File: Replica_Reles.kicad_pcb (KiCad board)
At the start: 2 copper layers, 60 x 145 mm, 70 parts, among them J1 Bornera, J2 Bornera, J3 Tira de Pines Macho, J4 Bornera, J5 Bornera, J6 Bornera, J7 Bornera, J8 Bornera, J9 Bornera, K1 SONGLE_SRD_Form_C, K2 SONGLE_SRD_Form_C, K3 SONGLE_SRD_Form_C, K4 SONGLE_SRD_Form_C, K5 SONGLE_SRD_Form_C, K6 SONGLE_SRD_Form_C, K7 SONGLE_SRD_Form_C, K8 SONGLE_SRD_Form_C, Q1 S8050, Q2 S8050, Q3 S8050, Q4 S8050, Q5 S8050, Q6 S8050, Q7 S8050, Q8 S8050, U1 PC817, U2 PC817, U3 PC817, U4 PC817, U5 PC817, U6 PC817, U7 PC817, U8 PC817

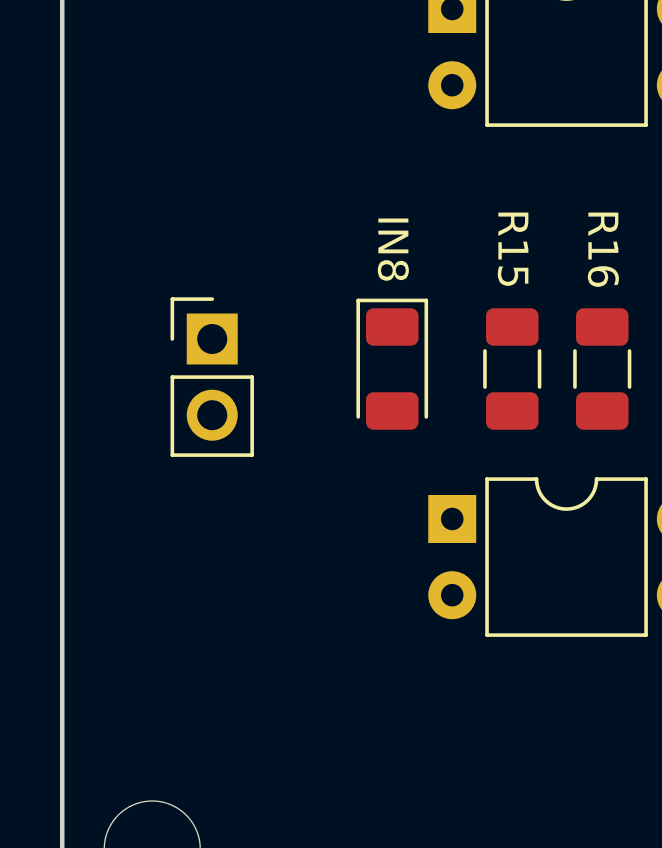
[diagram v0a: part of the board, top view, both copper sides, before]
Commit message: Arreglo de modelos 3D
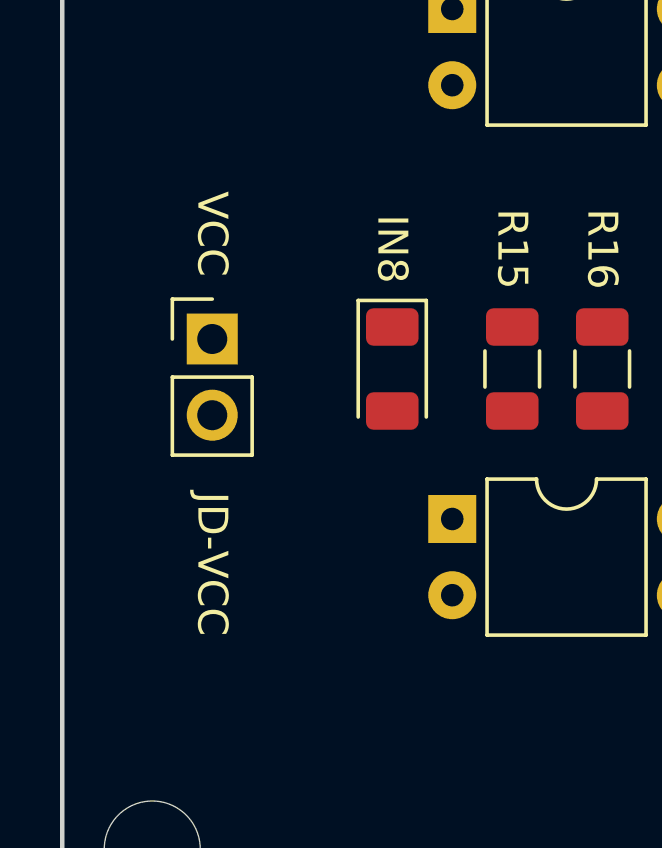
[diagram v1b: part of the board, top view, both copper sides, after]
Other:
- board text added: "JD-VCC"
- board text added: "VCC"
